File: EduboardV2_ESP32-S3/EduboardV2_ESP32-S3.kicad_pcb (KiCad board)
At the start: 4 copper layers, 35 x 63.3 mm, 53 parts, among them J1 EduboardV2 PCIE UP Board Conn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, Q1 L8050QLT1G, Q2 L8050QLT1G, Q3 AO3401A, SW1 K2-1102SP-C4SC-04, SW2 K2-1102SP-C4SC-04, U1 ESP32-S3-WROOM-1(N8R2), U2 CP2102N-A02-GQFN28R, U5 LD1117S33TR_SOT223

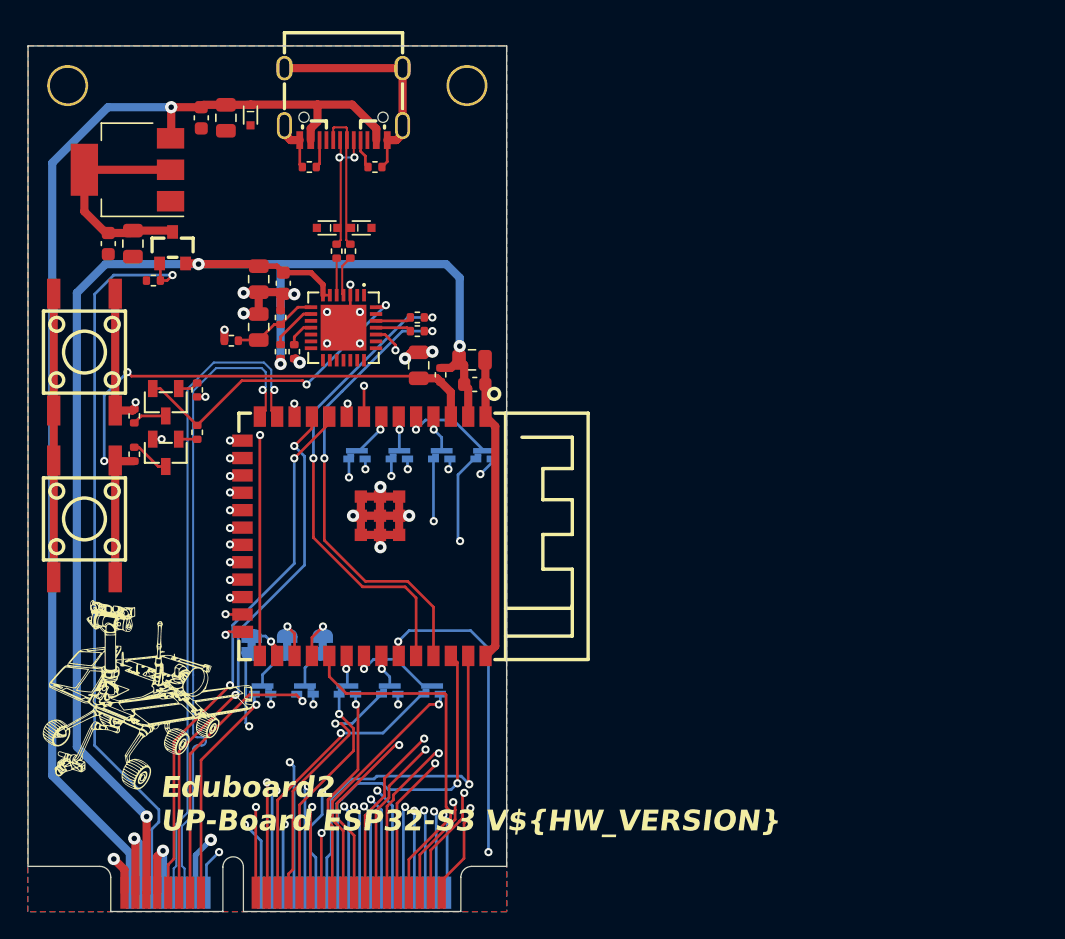
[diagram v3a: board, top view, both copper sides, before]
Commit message: Do all modifications for V1.1 and create production data
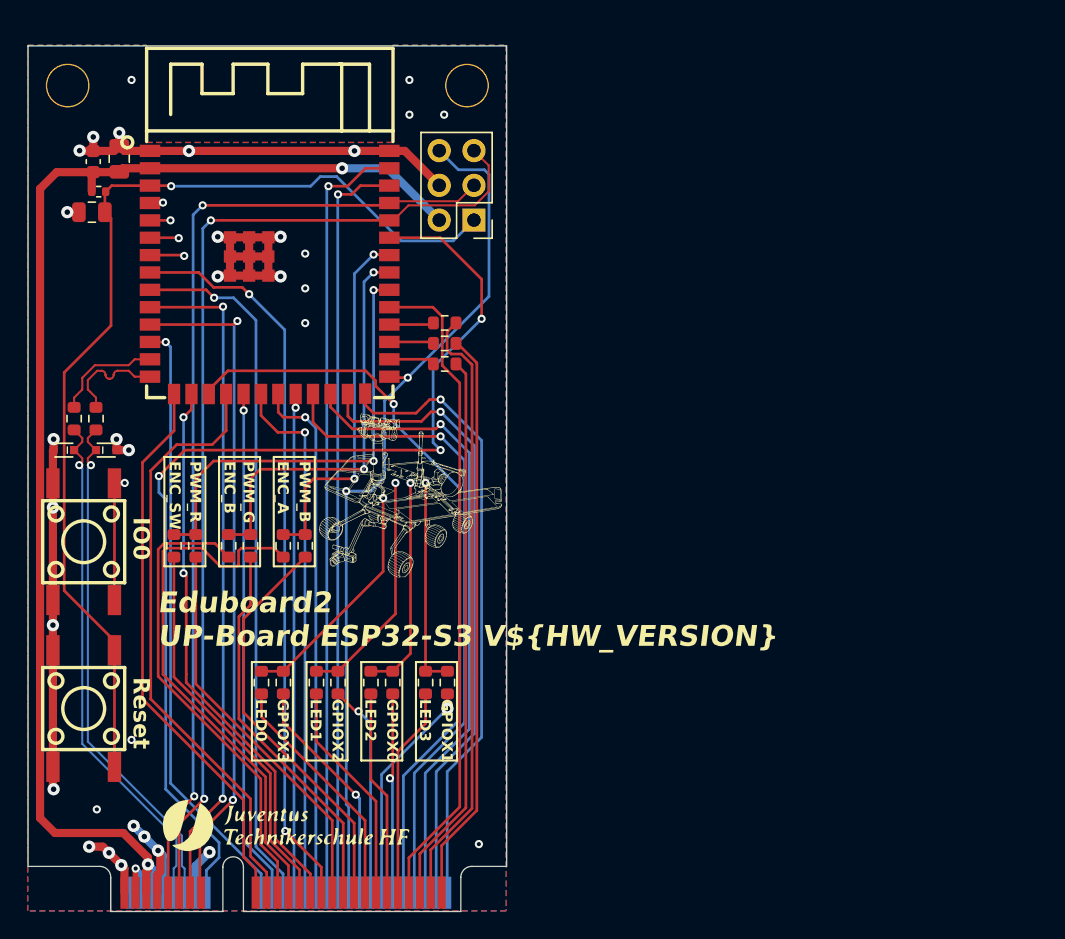
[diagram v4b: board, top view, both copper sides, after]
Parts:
- removed C25, C27, C4: 4u7, Capacitor_SMD:C_0805_2012Metric
- removed C26, C28, C5: 100n, Capacitor_SMD:C_0603_1608Metric
- removed C6: 1u, Capacitor_SMD:C_0805_2012Metric
- removed D3: LESD5D5.0CT1G, EduboardV2_kicadlib:SOD-523_L1.2-W0.8-LS1.6-BI
- removed the G*** at (109.3, 141.6)
- removed the G*** at (132.3, 104.4)
- removed JP1, JP2, JP3: SolderJumper_2_Bridged, Jumper:SolderJumper-2_P1.3mm_Bridged_RoundedPad1.0x1.5mm
- removed JP10, JP4, JP5, JP6, JP7, JP8, JP9: SolderJumper_3_Bridged12, EduboardV2_kicadlib:SolderJumper_Small-3_bridged12
- removed JP11, JP12: SolderJumper_3_Bridged12, EduboardV2_kicadlib:SolderJumper_Small-3_bridged23
- removed Q1, Q2: L8050QLT1G, EduboardV2_kicadlib:SOT-23-3_L2.9-W1.3-P1.90-LS2.4-BR
- removed Q3: AO3401A, EduboardV2_kicadlib:SOT-23_L2.9-W1.3-P1.90-LS2.4-BR
- removed R25: 2k2, Resistor_SMD:R_0402_1005Metric
- removed R31, R32: 0R, Resistor_SMD:R_0402_1005Metric
- removed U2: CP2102N-A02-GQFN28R, EduboardV2_kicadlib:QFN-28_L5.0-W5.0-P0.50-TL-EP3.3
- removed U5: LD1117S33TR_SOT223, Package_TO_SOT_SMD:SOT-223-3_TabPin2
- removed USBC1: USB3.1C16PFSMT, EduboardV2_kicadlib:USB-C-SMD_TYPE-C-USB-17
- added G***: LOGO, EduboardV2_kicadlib:logo2, F.Cu at (104.1, 111.5)
- added G***: LOGO, EduboardV2_kicadlib:logo_opportunity2, F.Cu at (128.5, 127.0)
- added G***: LOGO, EduboardV2_kicadlib:JuventusLogo, F.Cu at (119.3, 151.1)
- added J2: Conn_02x03_Odd_Even, Connector_PinHeader_2.54mm:PinHeader_2x03_P2.54mm_Vertical, F.Cu at (133.1, 106.9)
- added R15: 0R, Resistor_SMD:R_0603_1608Metric, F.Cu at (111.2, 130.7)
- added R16: 0R, Resistor_SMD:R_0603_1608Metric, F.Cu at (103.9, 121.4)
- added R17: 0R, Resistor_SMD:R_0603_1608Metric, F.Cu at (105.5, 121.4)
- added R18: 0R, Resistor_SMD:R_0603_1608Metric, F.Cu at (131.0, 114.4)
- added R19: 0R, Resistor_SMD:R_0603_1608Metric, F.Cu at (131.0, 115.9)
- added R20: 0R, Resistor_SMD:R_0603_1608Metric, F.Cu at (131.0, 117.4)
- added R5: 0R, Resistor_SMD:R_0603_1608Metric, F.Cu at (123.2, 140.7)
- C1: value 100n -> 4u7; footprint Capacitor_SMD:C_0603_1608Metric -> Capacitor_SMD:C_0805_2012Metric
- C2: value 4u7 -> 100n; footprint Capacitor_SMD:C_0805_2012Metric -> Capacitor_SMD:C_0603_1608Metric
- R1: value 2k2 -> 10k
- R10, R13, R14, R9: footprint Resistor_SMD:R_0402_1005Metric -> Resistor_SMD:R_0603_1608Metric
- R11, R12, R2, R6, R7, R8: value 10k -> 0R; footprint Resistor_SMD:R_0402_1005Metric -> Resistor_SMD:R_0603_1608Metric
- R3: value 22k -> 0R; footprint Resistor_SMD:R_0402_1005Metric -> Resistor_SMD:R_0603_1608Metric
- R4: value 47k -> 0R; footprint Resistor_SMD:R_0402_1005Metric -> Resistor_SMD:R_0603_1608Metric
- moved R6 38.0 mm to (125.6, 140.7), turned to 90 degrees
- moved R7 37.7 mm to (127.2, 140.7), turned to 90 degrees
- moved C2 31.3 mm to (105.3, 102.6), turned to 90 degrees
- moved C1 30.8 mm to (107.2, 102.4), turned to -90 degrees
- moved D1 28.0 mm to (103.2, 123.7), turned to 0 degrees
- moved R4 26.8 mm to (121.6, 140.7), turned to 90 degrees
- moved R9 26.8 mm to (131.2, 140.7), turned to 90 degrees
- moved C3 26.4 mm to (105.2, 106.3), turned to 0 degrees
- moved R2 26.0 mm to (117.6, 140.7), turned to 90 degrees
- moved R8 26.0 mm to (129.6, 140.7)
- moved R3 25.3 mm to (119.2, 140.7), turned to 90 degrees
- moved D2 24.7 mm to (106.2, 123.7)
- moved U1 20.5 mm to (118.2, 110.7), turned to 0 degrees
- moved R1 17.7 mm to (105.7, 104.8), turned to 0 degrees
- moved R10 17.7 mm to (120.8, 130.7), turned to 90 degrees
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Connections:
- C1 pad 1: +3V3 -> GND
- C1 pad 2: GND -> +3V3
- C2 pad 1: GND -> +3V3
- C2 pad 2: +3V3 -> GND
- D1 pad 2: VBUS -> ESP_D-
- D2 pad 2: D+ -> ESP_D+
- J1 pad 11: ESP_U1_RX -> ESP_U0_RX
- J1 pad 13: ESP_U2_TX -> ESP_U1_TX
- J1 pad 15: ESP_U2_RX -> ESP_U1_RX
- J1 pad 6: 3.3V_Sense -> +3V3
- J1 pad 9: ESP_U1_TX -> ESP_U0_TX
- R1 pad 1: Net-(U2-RSTb) -> +3V3
- R1 pad 2: +3V3 -> ESP_EN
- R10 pad 1: ESP_U0_TX -> GPIO_PWM_B
- R10 pad 2: Net-(U2-RXD) -> ESP_GPIO41
- R11 pad 1: USB_UART_DTR -> GPIO_RotEnc_A
- R11 pad 2: Net-(Q1-B) -> ESP_GPIO41
- R12 pad 1: USB_UART_RTS -> GPIO_PWM_G
- R12 pad 2: Net-(Q2-B) -> ESP_GPIO40
- R13 pad 1: ESP_EN -> GPIO_RotEnc_B
- R13 pad 2: Net-(Q1-C) -> ESP_GPIO40
- R14 pad 1: ESP_GPIO0 -> GPIO_PWM_R
- R14 pad 2: Net-(Q2-C) -> ESP_GPIO39
- R2 pad 1: +3V3 -> GPIO_LED0
- R2 pad 2: ESP_EN -> ESP_GPIO4
- R3 pad 1: VBUS -> GPIOX3
- R3 pad 2: Net-(U2-VBUS) -> ESP_GPIO4
- R4 pad 1: GND -> GPIO_LED1
- R4 pad 2: Net-(U2-VBUS) -> ESP_GPIO5
- R6 pad 1: Net-(USBC1-CC2) -> GPIO_LED2
- R6 pad 2: GND -> ESP_GPIO6
- R7 pad 1: Net-(USBC1-CC1) -> GPIOX0
- R7 pad 2: GND -> ESP_GPIO6
- R8 pad 1: GND -> GPIO_LED3
- R8 pad 2: Net-(U2-SUSPENDb) -> ESP_GPIO7
- R9 pad 1: ESP_U0_RX -> GPIOX1
- R9 pad 2: Net-(U2-TXD) -> ESP_GPIO7
- U1 pad 13: ESP_D- -> D-
- U1 pad 14: ESP_D+ -> D+
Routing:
- net VBUS: track 106.6 -> 0.00 mm, vias 2 -> 0
- net 3.3V_Sense: track 54.5 -> 0.00 mm, vias 1 -> 0
- net ESP_GPIO4: track 2.75 -> 49.8 mm, vias 1 -> 2
- net ESP_GPIO6: track 2.53 -> 46.3 mm, vias 1 -> 2
- net ESP_GPIO7: track 3.34 -> 45.0 mm, vias 1 -> 2
- net ESP_GPIO5: track 7.16 -> 47.8 mm, vias 1 -> 2
- net ESP_U0_RX: track 34.9 -> 74.8 mm
- net ESP_U0_TX: track 34.0 -> 71.8 mm
- net GPIOX1: track 49.3 -> 16.5 mm, vias 2 -> 1
- net ESP_EN: track 44.0 -> 75.2 mm, vias 2 -> 1
- net GPIOX0: track 45.3 -> 14.7 mm, vias 2 -> 1
- net ESP_GPIO39: track 2.25 -> 32.9 mm, vias 1 -> 2
- net GPIOX3: track 47.5 -> 16.9 mm, vias 2 -> 1
- net GPIO_RS485_DE: track 46.5 -> 76.3 mm
- net GPIO_SCL: track 27.5 -> 56.7 mm
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- added copper zone on In1.Cu, net GND
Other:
- board text added: "ENC_A"
- board text added: "ENC_B"
- board text added: "ENC_SW"
- board text added: "GPIOX0"
- board text added: "GPIOX1"
- board text added: "GPIOX2"
- board text added: "GPIOX3"
- board text added: "IO0"
- board text added: "LED0"
- board text added: "LED1"
- board text added: "LED2"
- board text added: "LED3"
- board text added: "PWM_B"
- board text added: "PWM_G"
- board text added: "PWM_R"
- board text added: "Reset"
- board text removed: "ENC_A PWM_B"
- board text removed: "ENC_B PWM_G"
- board text removed: "ENC_SW PWM_R"
- board text removed: "JP1"
- board text removed: "JP2"
- board text removed: "JP3"
- board text removed: "LED0 GPIOX3"
- board text removed: "LED1 GPIOX2"
- board text removed: "LED2 GPIOX0"
- board text removed: "LED3 GPIOX1"
- board text removed: "U2_RX LED7"
- board text removed: "U2_TX LED6"
